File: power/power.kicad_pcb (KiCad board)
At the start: 2 copper layers, 100 x 100 mm, 40 parts, among them K1 MASTER_LIVE, K2 PREHEAT, M3_MOUNT VAL**, P1 CONTROL, P2 MAINS_INLET, P3 LOAD_OUTLET, P4 +5V, P5 GND, P6 I_SENSE, Q1 BC817-40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

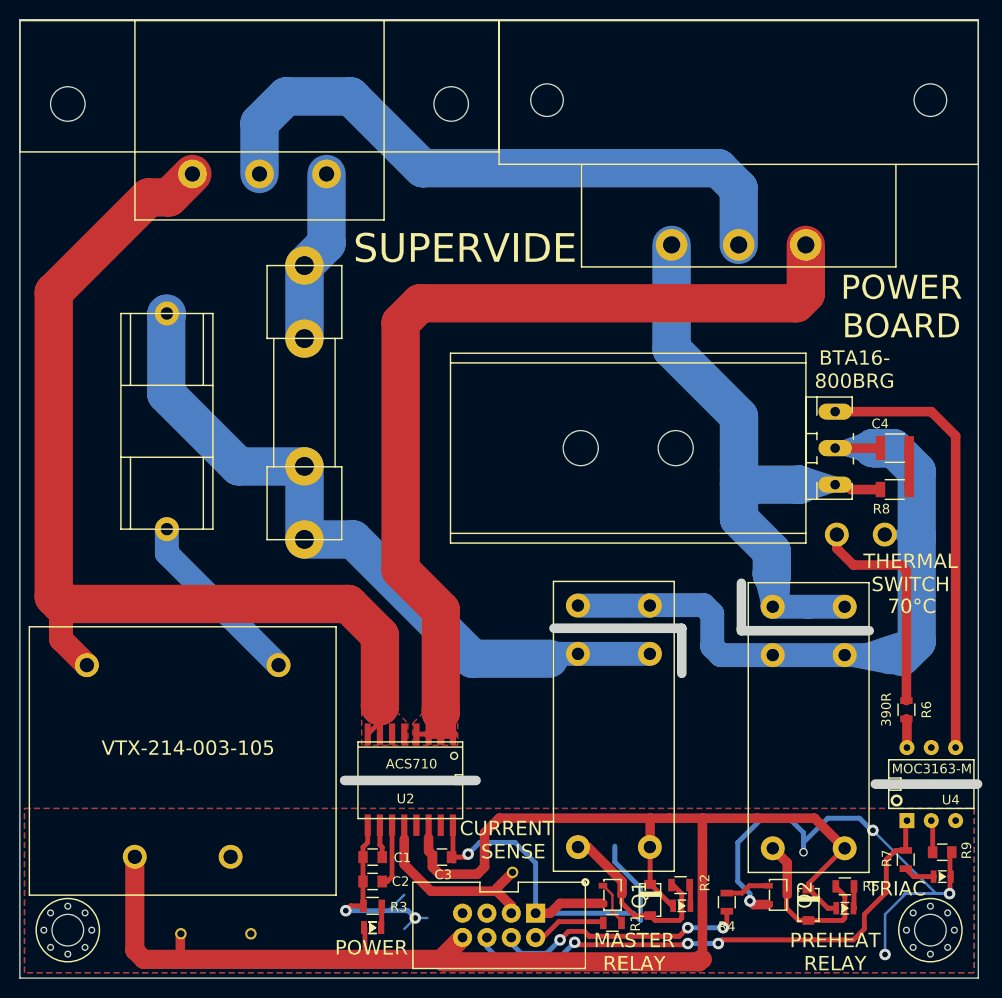
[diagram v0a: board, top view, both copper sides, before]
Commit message: Added voltage warning, bumped rev+date
Resolves #23 and resolves #6
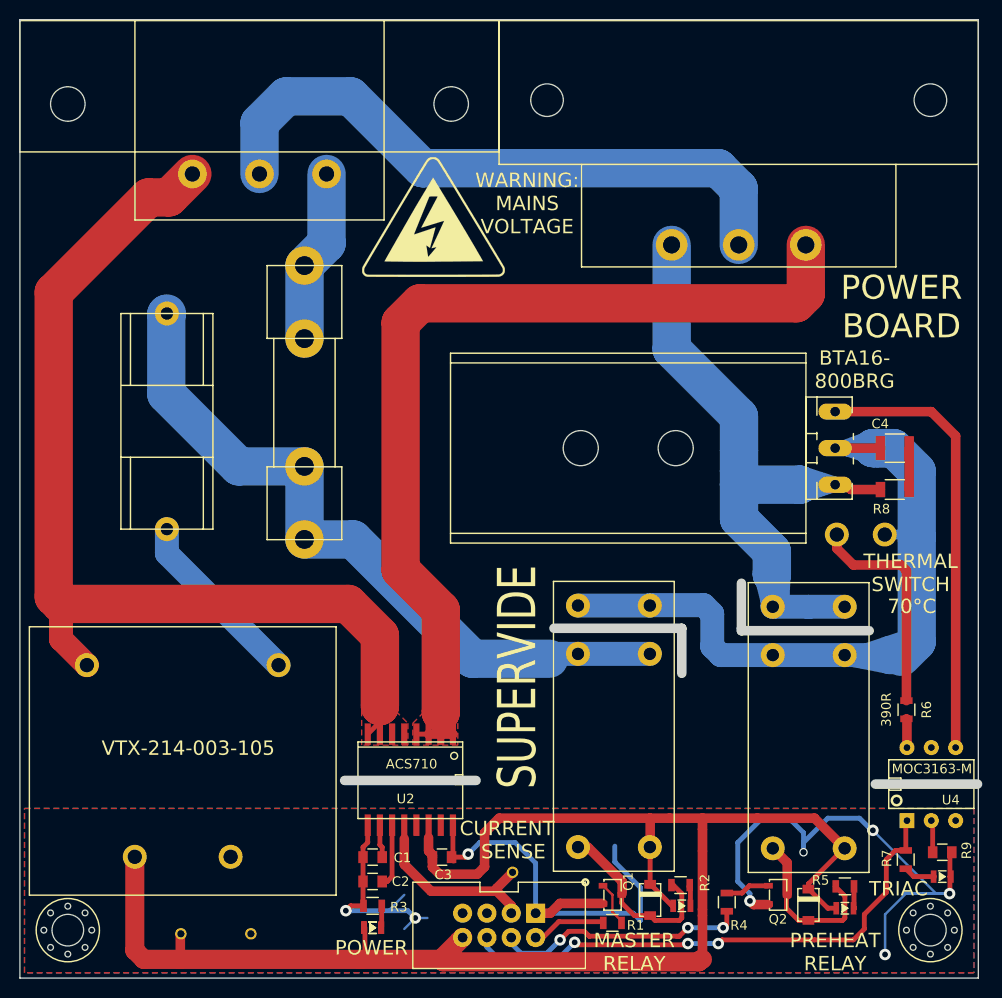
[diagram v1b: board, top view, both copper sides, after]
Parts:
- added G***: LOGO, power:voltage_warn, F.Cu at (73.2, 52.6)
- added G***: LOGO, power:voltage_warn, B.Cu at (79.0, 58.7)
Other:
- board text added: "2015-10-04 REVISION 2"
- board text added: "DAVID TURNER ADAM GREIG JON SOWMAN"
- board text added: "WARNING: MAINS VOLTAGE"
- board text removed: "2015-03-30 REVISION 1"
- board text removed: "POWER BOARD DAVID TURNER ADAM GREIG JON SOWMAN"

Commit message: Many minor fixes, resolves #25
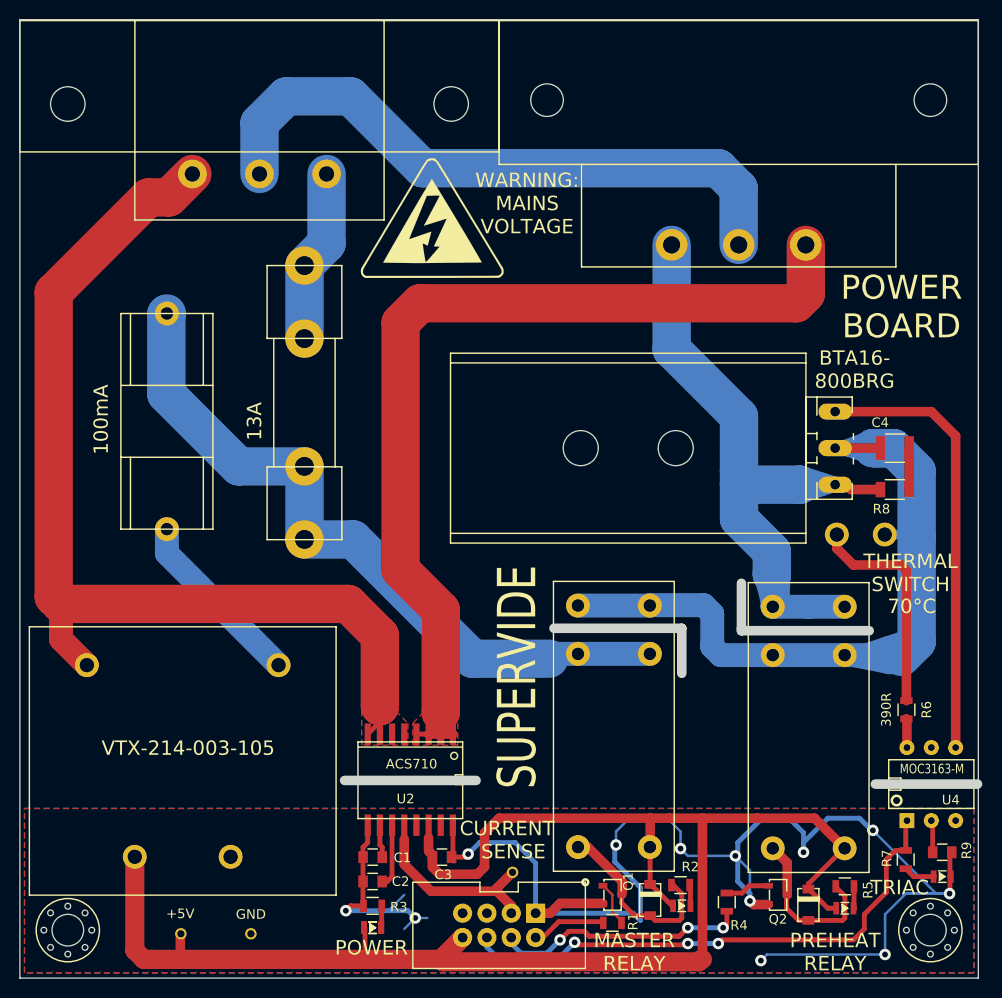
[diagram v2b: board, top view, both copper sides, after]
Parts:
- removed the G*** at (73.2, 52.6)
- removed the G*** at (79.0, 58.7)
- added G***: LOGO, power:voltage_warn, B.Cu at (79.4, 58.8)
- added G***: LOGO, power:voltage_warn, F.Cu at (73.0, 52.7)
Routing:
- net GND: track 136.4 -> 171.9 mm, vias 8 -> 12
